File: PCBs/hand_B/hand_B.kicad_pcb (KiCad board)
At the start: 2 copper layers, 52.6 x 37.4 mm, 5 parts

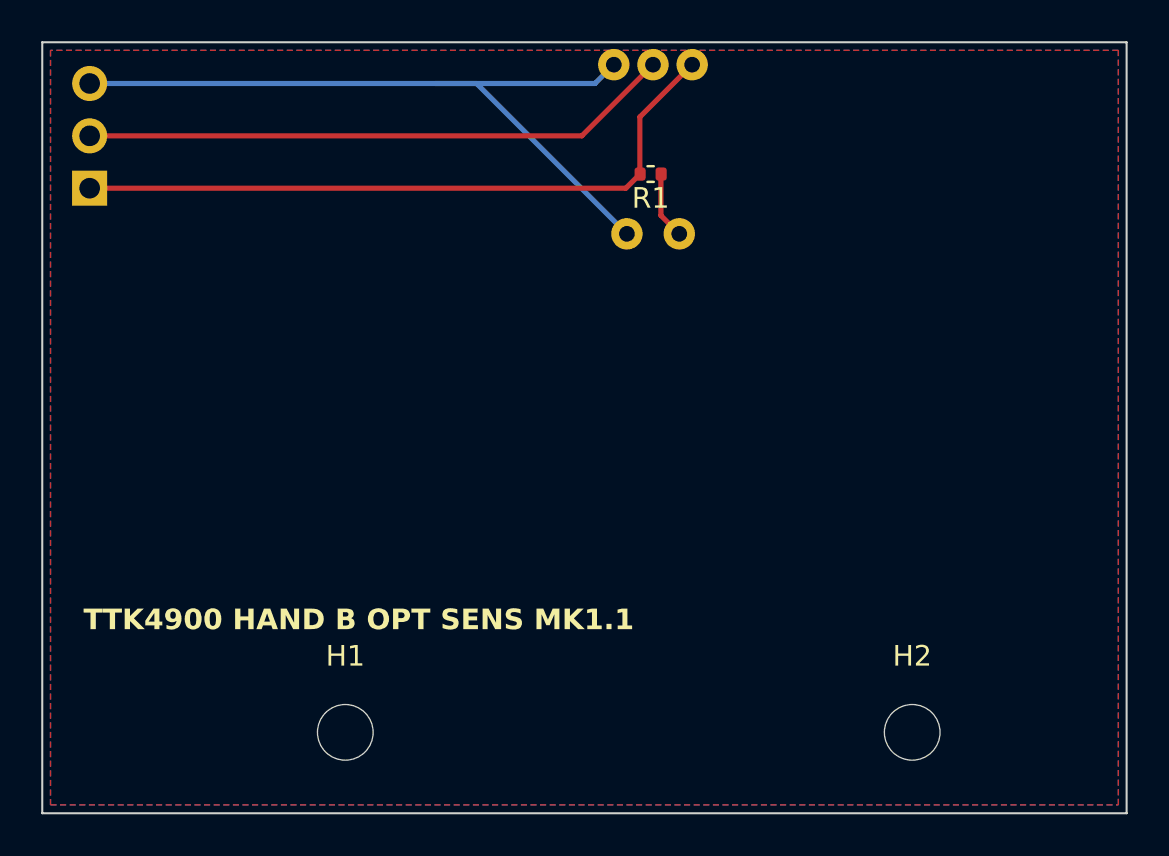
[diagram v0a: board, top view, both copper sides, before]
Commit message: Working UART input for basic control. All motors work. Next up: switch interrupts
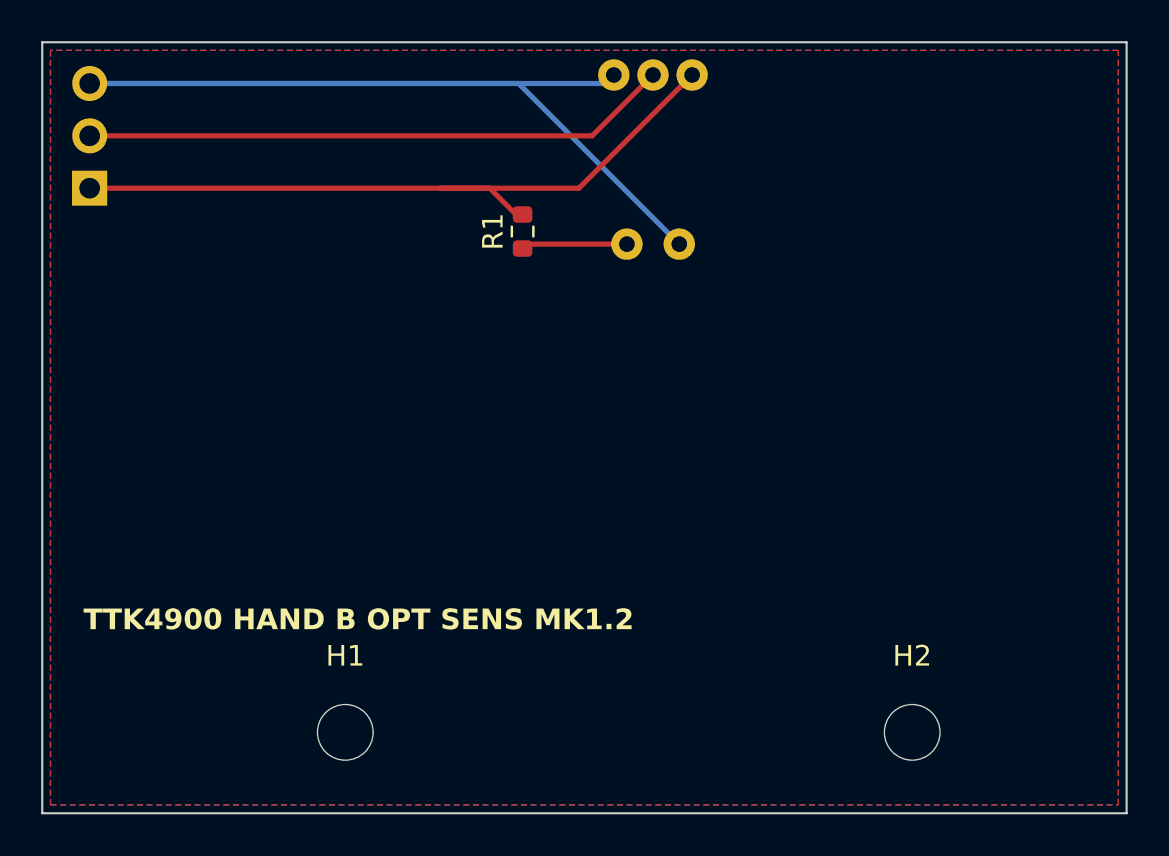
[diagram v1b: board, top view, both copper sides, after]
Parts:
- R1: footprint Resistor_SMD:R_0402_1005Metric -> Resistor_SMD:R_0603_1608Metric
- moved R1 6.81 mm to (97.1, 41.7), turned to 90 degrees
- moved OPT1 0.50 mm to (104.7, 37.2)
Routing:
- net /5V: track 38.1 -> 57.4 mm
- net /0v: track 33.3 -> 36.0 mm
- net Net-(OPT1-Cathode): track 3.26 -> 5.29 mm
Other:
- board text added: "TTK4900 HAND B OPT SENS MK1.2"
- board text removed: "TTK4900 HAND B OPT SENS MK1.1"
